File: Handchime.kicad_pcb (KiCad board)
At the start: 4 copper layers, 38.1 x 22.6 mm, 18 parts, among them J1 USB_C_Receptacle_USB2.0, J2 Pins, SW0 BOOT, SW1 Row 0, Col 0, SW2 Row 0, Col 1, U1 CH552T, U2 PRTR5V0U2X

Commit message: Rename from HandCHime to Handchime
With FAK development being discontinued, it no longer makes sense to use the **CH**552T. With an STM32, HandSTamp would make sense, but there are already a number of projects with “stamp”-based names. So the “Handchime” name stays, but without the emphasis on the “CH” part.
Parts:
- J2: footprint Project Library:HandCHime -> Project Library:Handchime
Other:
- board text added: "Handchime"
- board text removed: "HandCHime"
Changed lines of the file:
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@@
 		(property ki_fp_filters "C_*")
 		(sheetname "Root")
-		(sheetfile "HandCHime.kicad_sch")
+		(sheetfile "Handchime.kicad_sch")
 		(attr smd)
 		(duplicate_pad_numbers_are_jumpers no)
@@
 		(property ki_fp_filters "Net*Tie*")
 		(sheetname "Root")
-		(sheetfile "HandCHime.kicad_sch")
+		(sheetfile "Handchime.kicad_sch")
 		(attr exclude_from_pos_files exclude_from_bom allow_missing_courtyard)
 		(net_tie_pad_groups "1, 2")
@@
 		(property ki_fp_filters "R_*")
 		(sheetname "Root")
-		(sheetfile "HandCHime.kicad_sch")
+		(sheetfile "Handchime.kicad_sch")
 		(attr smd)
 		(duplicate_pad_numbers_are_jumpers no)
@@
 		(property ki_fp_filters "SOT?143*")
 		(sheetname "Root")
-		(sheetfile "HandCHime.kicad_sch")
+		(sheetfile "Handchime.kicad_sch")
 		(attr smd)
 		(duplicate_pad_numbers_are_jumpers no)
@@
 		)
 		(sheetname "Root")
-		(sheetfile "HandCHime.kicad_sch")
+		(sheetfile "Handchime.kicad_sch")
 		(attr smd)
 		(duplicate_pad_numbers_are_jumpers no)
@@
 		(property ki_fp_filters "*polyfuse* *PTC*")
 		(sheetname "Root")
-		(sheetfile "HandCHime.kicad_sch")
+		(sheetfile "Handchime.kicad_sch")
 		(attr smd)
 		(duplicate_pad_numbers_are_jumpers no)
@@
 		(property ki_fp_filters "TO-???* *_Diode_* *SingleDiode* D_*")
 		(sheetname "Root")
-		(sheetfile "HandCHime.kicad_sch")
+		(sheetfile "Handchime.kicad_sch")
 		(attr smd)
 		(duplicate_pad_numbers_are_jumpers no)
@@
 		(property ki_fp_filters "TO-???* *_Diode_* *SingleDiode* D_*")
 		(sheetname "Root")
-		(sheetfile "HandCHime.kicad_sch")
+		(sheetfile "Handchime.kicad_sch")
 		(attr smd)
 		(duplicate_pad_numbers_are_jumpers no)
@@
 		(property ki_fp_filters "Jumper* TestPoint*2Pads* TestPoint*Bridge*")
 		(sheetname "Root")
-		(sheetfile "HandCHime.kicad_sch")
+		(sheetfile "Handchime.kicad_sch")
 		(attr exclude_from_pos_files allow_missing_courtyard)
 		(net_tie_pad_groups "1, 2")
@@
 		(property ki_fp_filters "R_*")
 		(sheetname "Root")
-		(sheetfile "HandCHime.kicad_sch")
+		(sheetfile "Handchime.kicad_sch")
 		(attr smd)
 		(duplicate_pad_numbers_are_jumpers no)
@@
 		(property ki_fp_filters "C_*")
 		(sheetname "Root")
-		(sheetfile "HandCHime.kicad_sch")
+		(sheetfile "Handchime.kicad_sch")
 		(attr smd)
 		(duplicate_pad_numbers_are_jumpers no)
@@
 		)
 	)
-	(footprint "Project Library:HandCHime"
+	(footprint "Project Library:Handchime"
 		(layer "F.Cu")
 		(at 158.75 58.928)
@@
 		)
 		(sheetname "Root")
-		(sheetfile "HandCHime.kicad_sch")
+		(sheetfile "Handchime.kicad_sch")
 		(attr through_hole exclude_from_bom)
 		(duplicate_pad_numbers_are_jumpers no)
@@
 		(property ki_fp_filters "USB*C*Receptacle*")
 		(sheetname "Root")
-		(sheetfile "HandCHime.kicad_sch")
+		(sheetfile "Handchime.kicad_sch")
 		(attr smd)
 		(duplicate_pad_numbers_are_jumpers no)
@@
 		(property ki_fp_filters "R_*")
 		(sheetname "Root")
-		(sheetfile "HandCHime.kicad_sch")
+		(sheetfile "Handchime.kicad_sch")
 		(attr smd)
 		(duplicate_pad_numbers_are_jumpers no)
@@
 		(property ki_fp_filters "TO-???* *_Diode_* *SingleDiode* D_*")
 		(sheetname "Root")
-		(sheetfile "HandCHime.kicad_sch")
+		(sheetfile "Handchime.kicad_sch")
 		(attr smd)
 		(duplicate_pad_numbers_are_jumpers no)
@@
 		)
 		(sheetname "Root")
-		(sheetfile "HandCHime.kicad_sch")
+		(sheetfile "Handchime.kicad_sch")
 		(attr smd)
 		(duplicate_pad_numbers_are_jumpers no)
@@
 		)
 		(sheetname "Root")
-		(sheetfile "HandCHime.kicad_sch")
+		(sheetfile "Handchime.kicad_sch")
 		(attr through_hole exclude_from_pos_files)
 		(duplicate_pad_numbers_are_jumpers no)
@@
 		)
 		(sheetname "Root")
-		(sheetfile "HandCHime.kicad_sch")
+		(sheetfile "Handchime.kicad_sch")
 		(attr through_hole exclude_from_pos_files)
 		(duplicate_pad_numbers_are_jumpers no)
@@
 		)
 	)
-	(gr_text "HandCHime"
+	(gr_text "Handchime"
 		(at 147.955 57.15 0)
 		(layer "F.Mask")
@@
 			)
 		)
-		(render_cache "HandCHime" 0
+		(render_cache "Handchime" 0
 			(polygon
 				(pts

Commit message: Update PCB with STH32 version draft
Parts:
- removed NT2: NetTie_2, Project Library:NetTie-2_SMD_Pad0.254mm
- removed R3: 5.1k, Resistor_SMD:R_0603_1608Metric
- added C3: 4.7µF, Capacitor_SMD:C_0603_1608Metric, F.Cu at (155.7, 57.1)
- added C4: 100nF, Capacitor_SMD:C_0603_1608Metric, F.Cu at (158.8, 57.1)
- added C5: 100nF, Capacitor_SMD:C_0603_1608Metric, F.Cu at (161.8, 57.1)
- added J3: SWD, TestPoint:TestPoint_Pad_D1.0mm, F.Cu at (151.6, 52.3)
- added R4: 10kΩ, Resistor_SMD:R_0603_1608Metric, F.Cu at (155.4, 49.4)
- added R5: 330Ω, Resistor_SMD:R_0603_1608Metric, F.Cu at (145.7, 54.1)
- added U3: XC6206P332MR-G, Package_TO_SOT_SMD:SOT-23-3, F.Cu at (143.1, 49.8)
- C1, C2: value 100nF -> 1µF
- D1: footprint Project Library:D_SOD-323 -> BGK_Kicad:D_SOD-323
- J1: value USB_C_Receptacle_USB2.0 -> USB_C_Receptacle_USB2.0_16P; footprint Connector_USB:USB_C_Receptacle_GCT_USB4105-xx-A_16P_TopMnt_Horizontal -> Connector_USB:USB_C_Receptacle_HRO_TYPE-C-31-M-12
- NT1: moved to B.Cu
- SW0: footprint Project Library:SW_SPST_B3U-1000P -> Button_Switch_SMD:SW_SPST_B3U-1000P
- U1: value CH552T -> STM32C071GBUx; footprint Package_SO:TSSOP-20_4.4x6.5mm_P0.65mm -> Package_DFN_QFN:QFN-28_4x4mm_P0.5mm
- moved C1 19.3 mm to (145.5, 47.8)
- moved SW0 19.1 mm to (149.2, 54.5), turned to 180 degrees
- moved C2 18.8 mm to (145.7, 51.1), turned to 90 degrees
- moved R2 2.13 mm to (150.9, 43.2)
- moved NT1 2.01 mm to (158.8, 47.6), turned to -90 degrees
- moved U1 1.78 mm to (159.0, 52.2), turned to 90 degrees
- moved R1 1.74 mm to (152.4, 43.2), turned to -90 degrees
- moved D2 1.23 mm to (174.8, 44.0), turned to 90 degrees
- moved D3 1.23 mm to (142.7, 44.0), turned to 90 degrees
- moved F1 0.71 mm to (164.1, 47.8)
- moved D1 0.61 mm to (162.3, 47.8)
- moved U2 0.25 mm to (158.8, 47.8)
- moved J1 0.18 mm to (158.7, 40.7)
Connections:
- J1 pad A1: GNDPWR -> ISLAND
- J1 pad A12: GNDPWR -> ISLAND
- J1 pad B1: GNDPWR -> ISLAND
- J1 pad B12: GNDPWR -> ISLAND
- J2 pad 1: R0 -> VCC
- J2 pad 10: P10 -> PB7
- J2 pad 11: P11 -> PB8
- J2 pad 12: P13 -> C1
- J2 pad 13: P33 -> PA0
- J2 pad 14: C0 -> PA1
- J2 pad 15: GND -> PA2
- J2 pad 16: TX -> PA3
- J2 pad 17: RX -> PA4
- J2 pad 18: +3V3 -> C0
- J2 pad 19: VCC -> PA5
- J2 pad 2: GND -> +3V3
- J2 pad 20: P35 -> PA6
- J2 pad 21: GND -> PA7
- J2 pad 22: R0 -> PB0
- J2 pad 3: P14 -> GND
- J2 pad 4: VCC -> R0
- J2 pad 5: P15 -> PA15
- J2 pad 6: P16 -> PB3
- J2 pad 7: P17 -> PB4
- J2 pad 8: GND -> PB5
- J2 pad 9: C1 -> PB6
- NT1 pad 1: GNDPWR -> ISLAND
- R1 pad 2: GNDPWR -> ISLAND
- R2 pad 2: GNDPWR -> ISLAND
- SW0 pad 1: Net-(R3-Pad2) -> BOOT0/SWCLK
- SW0 pad 2: +3V3 -> Net-(R5-Pad1)
- U1 pad 10: TX -> PA4
- U1 pad 11: P33 -> PA5
- U1 pad 12: C0 -> PA6
- U1 pad 13: P35 -> PA7
- U1 pad 14: USB+ -> PB0
- U1 pad 15: USB- -> R0
- U1 pad 16: P13 -> C0
- U1 pad 17: R0 -> unconnected-(U1-PC6-Pad17)
- U1 pad 18: GND -> USB-
- U1 pad 19: VCC -> USB+
- U1 pad 2: P14 -> unconnected-(U1-PC15-Pad2)
- U1 pad 20: +3V3 -> SWDIO
- U1 pad 3: P15 -> +3V3
- U1 pad 4: P16 -> GND
- U1 pad 5: P17 -> NRST
- U1 pad 6: RST -> PA0
- U1 pad 7: P10 -> PA1
- U1 pad 8: P11 -> PA2
- U1 pad 9: RX -> PA3
- U2 pad 1: GNDPWR -> ISLAND
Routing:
- net PA15: track 0.00 -> 24.2 mm, vias 0 -> 1
- net RX: track 21.4 -> 0.00 mm, vias 1 -> 0
- net P35: track 21.1 -> 0.00 mm, vias 2 -> 0
- net TX: track 20.9 -> 0.00 mm, vias 1 -> 0
- net PB4: track 0.00 -> 20.6 mm
- net PB3: track 0.00 -> 20.4 mm
- net PB0: track 0.00 -> 19.8 mm
- net PA6: track 0.00 -> 18.8 mm
- net P14: track 18.4 -> 0.00 mm
- net PA7: track 0.00 -> 18.0 mm
- net PB5: track 0.00 -> 17.6 mm
- net PA5: track 0.00 -> 17.1 mm
- net P15: track 16.2 -> 0.00 mm
- net P17: track 16.0 -> 0.00 mm
- net P16: track 15.8 -> 0.00 mm
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- added copper zone on In2.Cu, net GND
- added copper zone on B.Cu, net ISLAND
- added copper zone on F.Cu, net ISLAND
- added copper zone on In1.Cu, net ISLAND
- added copper zone on In2.Cu, net ISLAND
- removed copper zone on B.Cu, net GNDPWR
- removed copper zone on F.Cu, net GNDPWR
- removed copper zone on In1.Cu, net GNDPWR
- removed copper zone on In2.Cu, net GNDPWR
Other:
- board size 38.1 x 22.6 mm -> 40.6 x 21.5 mm
- board text added: "USB Port Y should be 42.164mm"
- board text added: "v2.0 • bgkendall"
- board text removed: "v1.0 • bgkendall"

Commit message: Various tweaks and improvements
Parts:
- moved R1 1.60 mm to (150.9, 43.6)
- moved R2 1.56 mm to (152.4, 43.6), turned to -90 degrees
- moved D2 0.84 mm to (175.0, 44.8)
- moved D3 0.84 mm to (142.5, 44.8)
- moved C1 0.28 mm to (145.4, 48.0), turned to -90 degrees
- moved C2 0.25 mm to (145.4, 51.1)
- moved R5 0.25 mm to (145.4, 54.1)
- moved U3 0.25 mm to (142.9, 49.8)
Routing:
- net GND: track 8.65 -> 23.6 mm, vias 6 -> 20
- net +3V3: track 29.2 -> 27.3 mm
- net Net-(J1-CC1): track 9.12 -> 11.1 mm
- net Net-(J1-CC2): track 8.02 -> 6.77 mm
- net VCC: track 45.6 -> 46.8 mm, vias 2 -> 3
- net VBUS: track 11.3 -> 10.4 mm
- net R0: track 56.1 -> 56.9 mm
- net PA15: track 24.2 -> 23.5 mm
- net C0: track 26.3 -> 26.4 mm, vias 1 -> 2
- net PA5: vias 0 -> 1

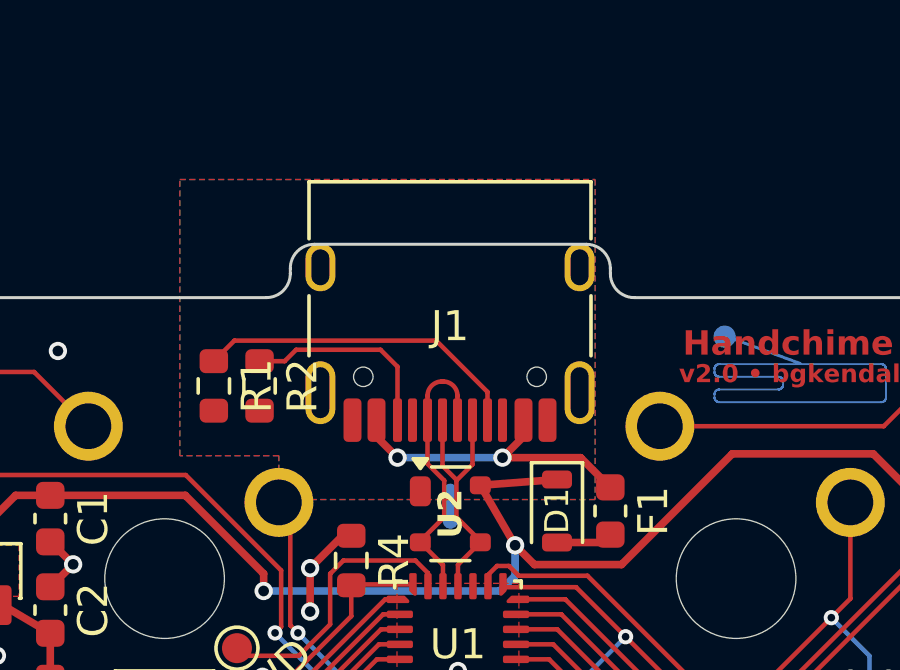
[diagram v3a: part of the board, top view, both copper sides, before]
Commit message: Move USB port into required location
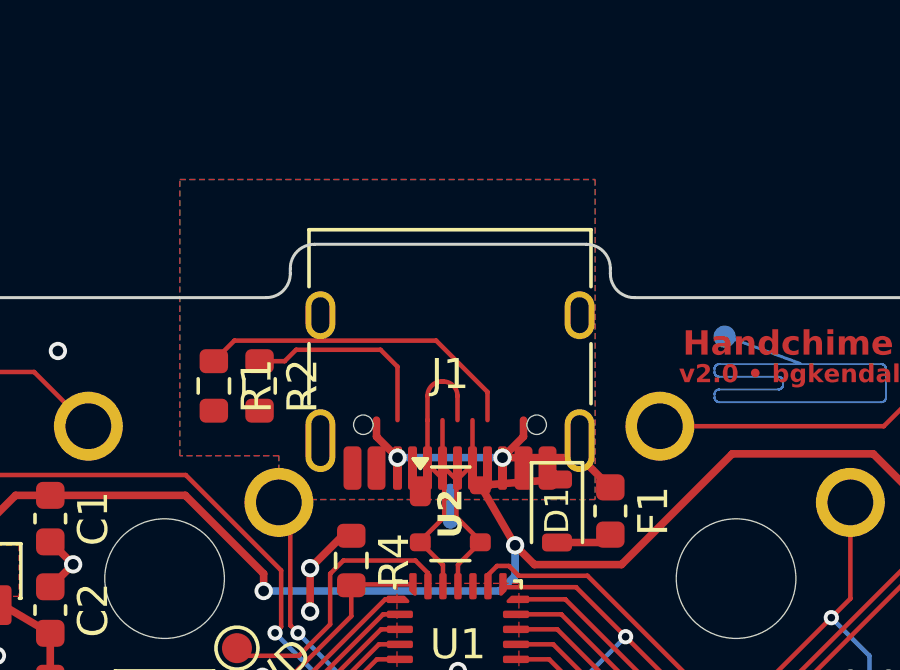
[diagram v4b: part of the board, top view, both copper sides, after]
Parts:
- moved J1 1.60 mm to (158.7, 42.3)
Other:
- board text added: "Alps pin 2"
- board text removed: "USB Port Y should be 42.164mm"
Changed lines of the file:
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@@
 	)
 	(footprint "Connector_USB:USB_C_Receptacle_HRO_TYPE-C-31-M-12"
+		(locked yes)
 		(layer "F.Cu")
-		(at 158.739 40.679 180)
+		(at 158.739 42.2763 180)
 		(descr "USB Type-C receptacle for USB 2.0 and PD, http://www.krhro.com/uploads/soft/180320/1-1P320120243.pdf")
 		(tags "usb usb-c 2.0 pd")
@@
 		(layer "B.Cu")
 	)
+	(gr_poly
+		(pts
+			(arc
+				(start 154.419 46.4563)
+				(mid 154.772553 46.309853)
+				(end 154.919 45.9563)
+			)
+			(arc
+				(start 154.919 44.8563)
+				(mid 154.772553 44.502747)
+				(end 154.419 44.3563)
+			)
+			(arc
+				(start 154.419 44.3563)
+				(mid 154.065447 44.502747)
+				(end 153.919 44.8563)
+			)
+			(arc
+				(start 153.919 45.9563)
+				(mid 154.065447 46.309853)
+				(end 154.419 46.4563)
+			)
+		)
+		(stroke
+			(width 0)
+			(type solid)
+		)
+		(fill yes)
+		(layer "Cmts.User")
+	)
+	(gr_line
+		(start 151.725 44.3563)
+		(end 154.419 44.3563)
+		(stroke
+			(width 0.04)
+			(type dot)
+		)
+		(layer "Cmts.User")
+	)
+	(gr_circle
+		(center 151.725 45.5063)
+		(end 152.875 45.5063)
+		(stroke
+			(width 0)
+			(type solid)
+		)
+		(fill yes)
+		(layer "Cmts.User")
+	)
 	(gr_line
 		(start 138.43 40.64)
@@
 		)
 	)
-	(gr_text "USB Port Y should be 42.164mm"
-		(at 158.739 36.322 0)
+	(gr_text "Alps pin 2"
+		(at 150.368 46.452371 90)
 		(layer "Cmts.User")
 		(effects
 			(font
-				(size 1 1)
-				(thickness 0.15)
+				(size 0.2 0.2)
 			)
-			(justify bottom)
+			(justify left bottom)
 		)
 	)

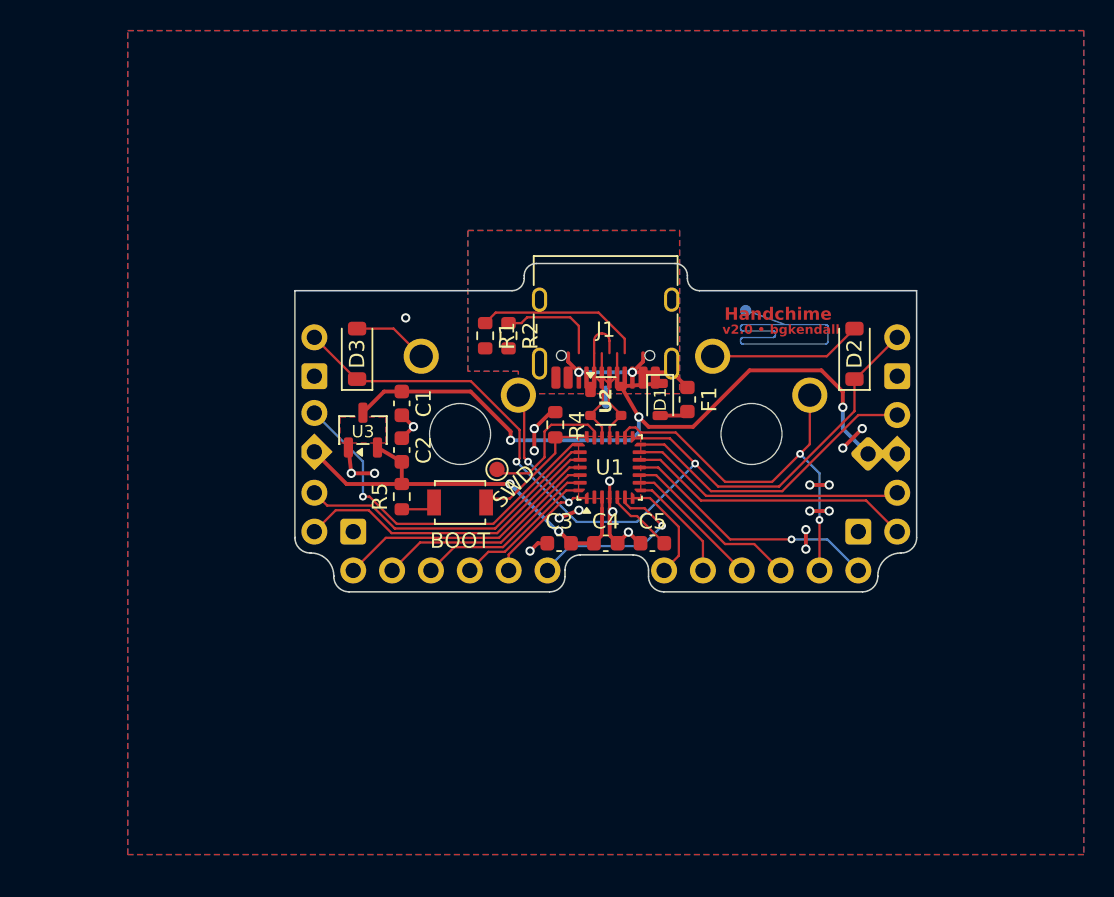
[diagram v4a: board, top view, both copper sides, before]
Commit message: Move board to align with MX grid
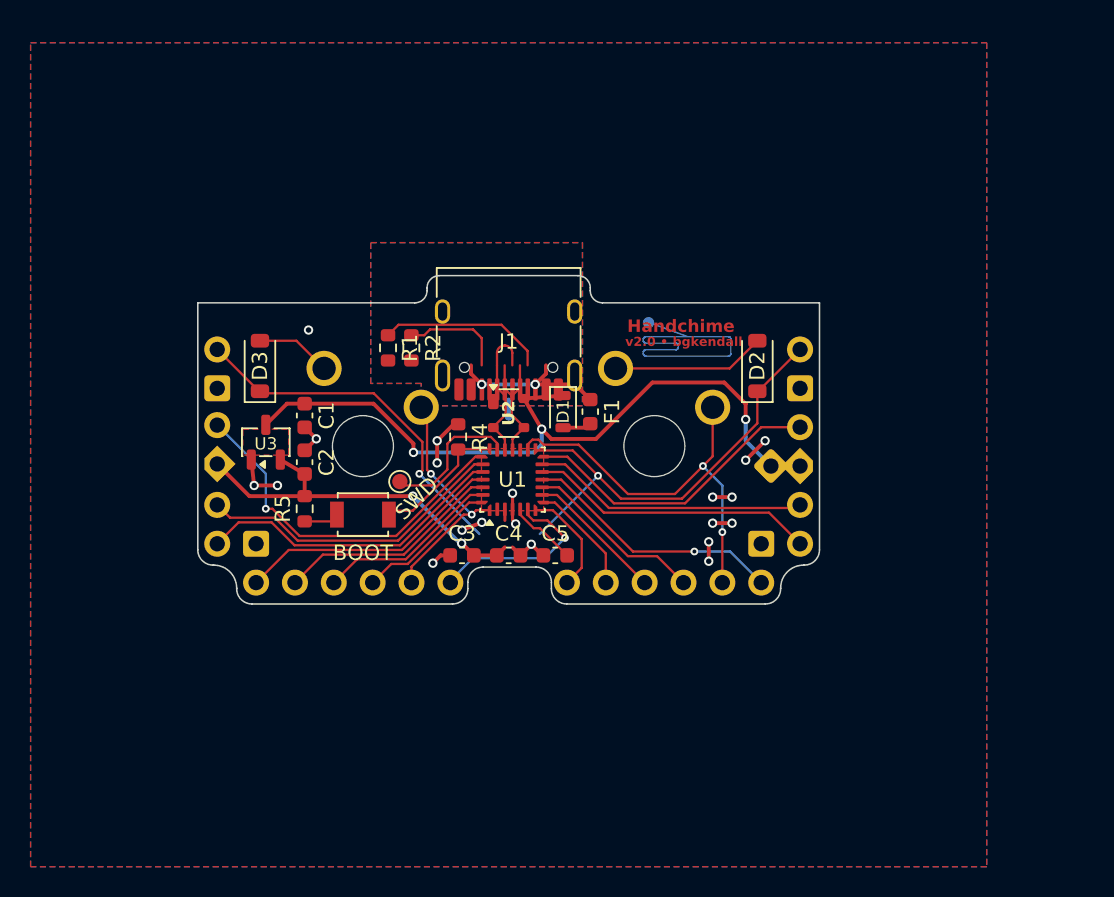
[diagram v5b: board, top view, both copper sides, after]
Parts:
- moved D1 6.40 mm to (156.0, 48.5)
- moved C1 6.40 mm to (139.1, 48.8)
- moved C2 6.40 mm to (139.1, 51.8)
- moved C3 6.40 mm to (149.4, 57.9)
- moved C4 6.40 mm to (152.4, 57.9)
- moved C5 6.40 mm to (155.4, 57.9)
- moved D2 6.40 mm to (168.7, 45.6)
- moved D3 6.40 mm to (136.1, 45.6)
- moved F1 6.40 mm to (157.7, 48.5)
- moved J2 6.40 mm to (152.4, 59.7)
- moved J3 6.40 mm to (145.3, 53.1)
- moved NT1 6.40 mm to (152.4, 48.4)
- moved R1 6.40 mm to (144.5, 44.4)
- moved R2 6.40 mm to (146.0, 44.4)
- moved R4 6.40 mm to (149.1, 50.2)
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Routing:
- net R0: track 56.9 -> 52.9 mm
- net GND: track 23.6 -> 21.8 mm
- net +3V3: track 27.3 -> 25.5 mm

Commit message: Move components to work with relocated USB port
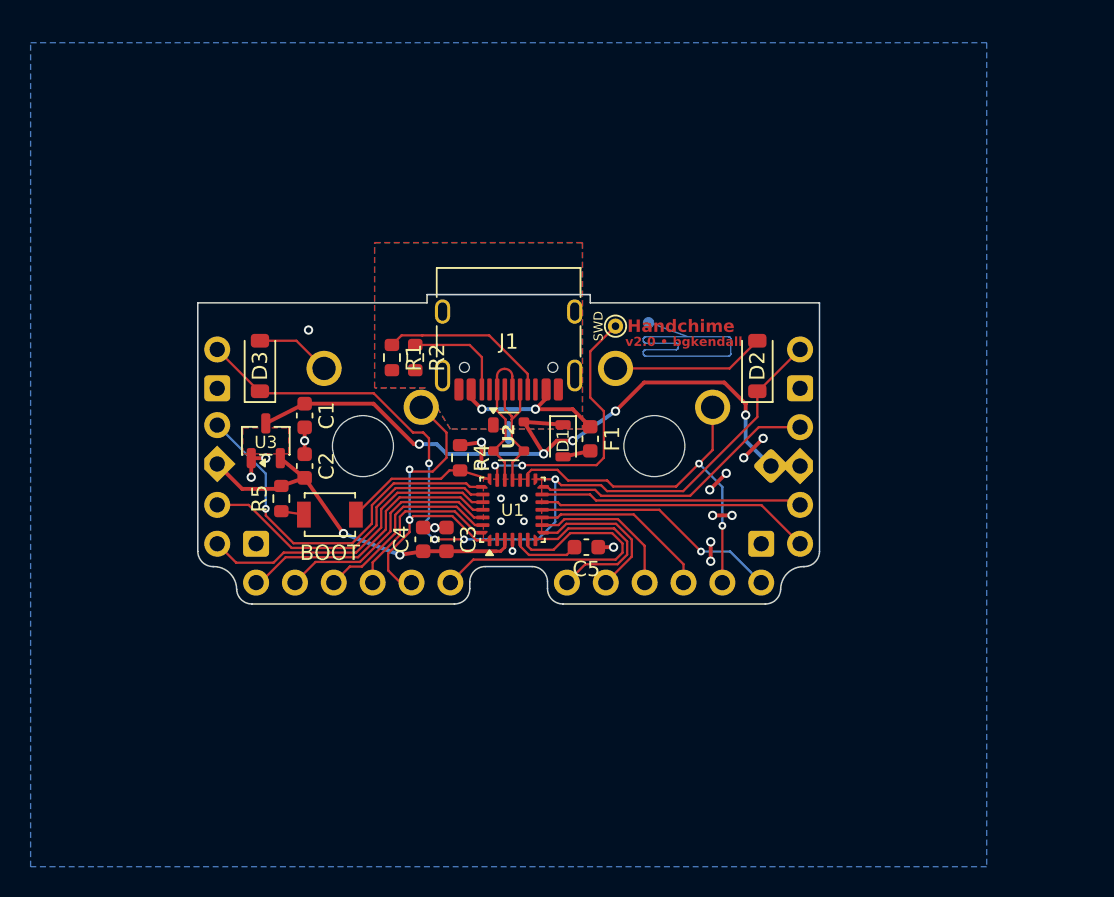
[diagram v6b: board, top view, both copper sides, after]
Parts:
- J3: footprint TestPoint:TestPoint_Pad_D1.0mm -> TestPoint:TestPoint_THTPad_D1.0mm_Drill0.5mm
- moved J3 17.4 mm to (159.4, 43.0), turned to -90 degrees
- moved C4 5.69 mm to (146.8, 56.9), turned to 90 degrees
- moved SW0 2.16 mm to (140.7, 55.3)
- moved C5 2.10 mm to (157.5, 57.4), turned to 0 degrees
- moved U1 1.97 mm to (152.7, 55.0)
- moved D1 1.91 mm to (156.0, 50.5)
- moved F1 1.78 mm to (157.7, 50.3)
- moved R5 1.66 mm to (137.5, 54.2)
- moved NT1 1.53 mm to (152.4, 49.9)
- moved U2 1.52 mm to (152.4, 50.2)
- moved C3 1.46 mm to (148.3, 56.9), turned to 90 degrees
- moved R4 1.37 mm to (149.2, 51.6)
- moved R1 0.68 mm to (144.8, 45.0)
- moved R2 0.68 mm to (146.3, 45.0)
- moved C2 0.25 mm to (139.1, 52.1)
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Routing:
- net SWDIO: track 9.39 -> 18.1 mm, vias 0 -> 2
- net PA0: track 12.2 -> 20.1 mm, vias 1 -> 0
- net GND: track 21.8 -> 16.0 mm, vias 20 -> 21
- net C1: track 16.1 -> 21.9 mm
- net PA1: track 7.05 -> 12.2 mm
- net R0: track 52.9 -> 56.8 mm, vias 2 -> 4
- net PA2: track 7.38 -> 9.99 mm
- net PB8: track 9.31 -> 11.1 mm
- net VCC: track 46.8 -> 45.1 mm, vias 3 -> 5
- net PB0: track 20.1 -> 18.9 mm
- net C0: track 26.4 -> 25.3 mm
- net BOOT0/SWCLK: track 8.87 -> 10.0 mm
- net +3V3: track 25.5 -> 24.5 mm
- net PA15: track 23.5 -> 24.5 mm
- net PA3: track 9.07 -> 9.99 mm
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- removed copper zone on In1.Cu, net GND
- removed copper zone on In2.Cu, net GND
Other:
- board size 40.6 x 21.5 mm -> 40.6 x 20.2 mm

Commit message: Various tweaks
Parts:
- moved R4 0.25 mm to (149.2, 51.3)
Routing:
- net GND: track 16.0 -> 15.3 mm, vias 21 -> 20
